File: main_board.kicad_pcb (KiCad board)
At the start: 2 copper layers, 158.5 x 153 mm, 15 parts, among them J1 MEGA_SARJ, J2 POWER, J3 I2C, J4 FREE_GPIO, J5 5V, J6 12V, J7 24V, J8 GND, J9 GND, U1 BNO055_IMU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

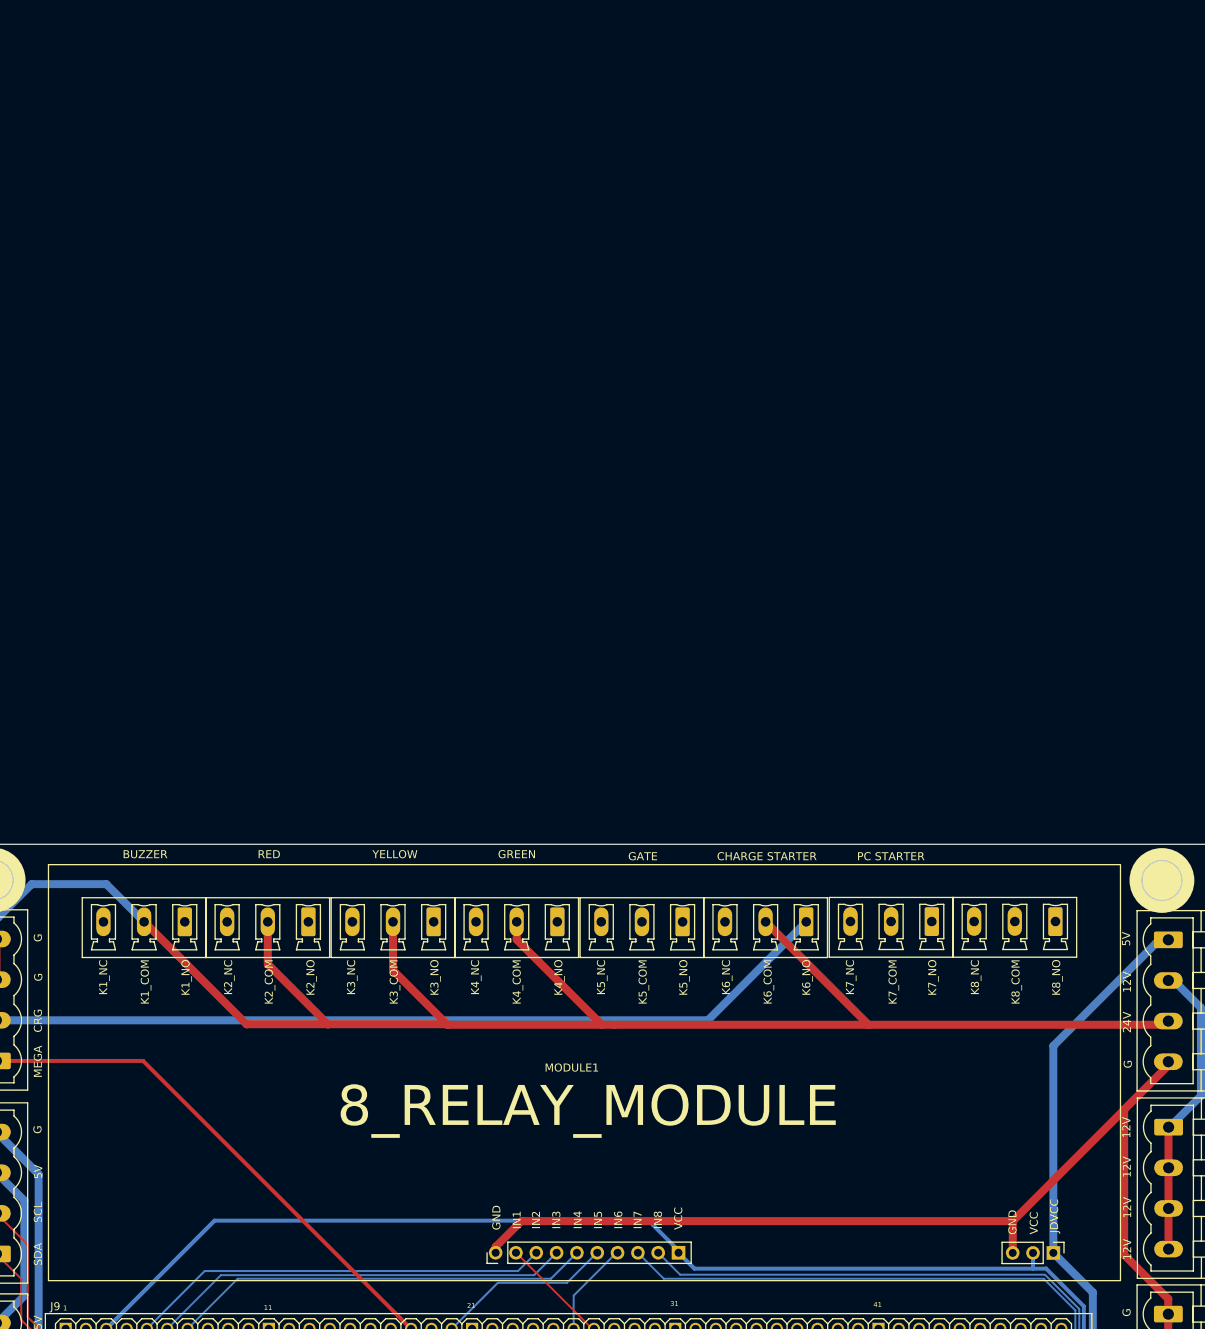
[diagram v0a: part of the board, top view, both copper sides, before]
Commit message: Deleting Relays Adding MOSFETs
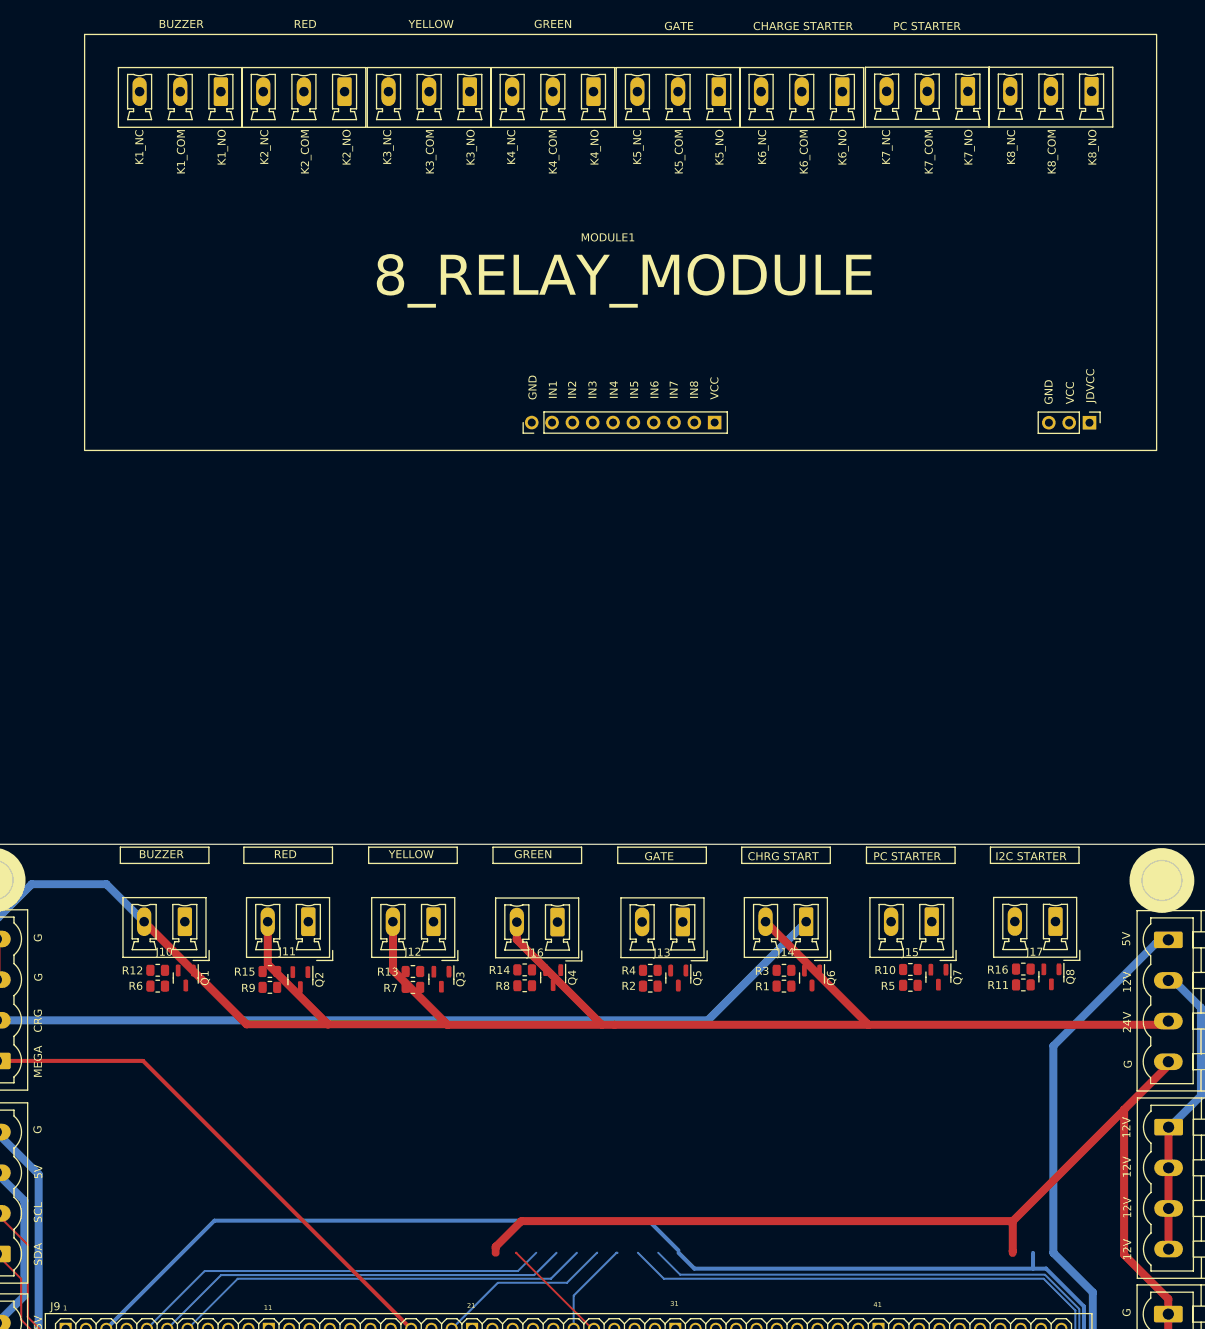
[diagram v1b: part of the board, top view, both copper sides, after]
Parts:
- added J10: Conn_01x02, Connector_Phoenix_MC_HighVoltage:PhoenixContact_MCV_1,5_2-G-5.08_1x02_P5.08mm_Vertical, F.Cu at (44.8, 26.2)
- added J11: Conn_01x02, Connector_Phoenix_MC_HighVoltage:PhoenixContact_MCV_1,5_2-G-5.08_1x02_P5.08mm_Vertical, F.Cu at (60.3, 26.2)
- added J12: Conn_01x02, Connector_Phoenix_MC_HighVoltage:PhoenixContact_MCV_1,5_2-G-5.08_1x02_P5.08mm_Vertical, F.Cu at (75.9, 26.2)
- added J13: Conn_01x02, Connector_Phoenix_MC_HighVoltage:PhoenixContact_MCV_1,5_2-G-5.08_1x02_P5.08mm_Vertical, F.Cu at (107.1, 26.2)
- added J14: Conn_01x02, Connector_Phoenix_MC_HighVoltage:PhoenixContact_MCV_1,5_2-G-5.08_1x02_P5.08mm_Vertical, F.Cu at (122.5, 26.2)
- added J15: Conn_01x02, Connector_Phoenix_MC_HighVoltage:PhoenixContact_MCV_1,5_2-G-5.08_1x02_P5.08mm_Vertical, F.Cu at (138.2, 26.2)
- added J16: Conn_01x02, Connector_Phoenix_MC_HighVoltage:PhoenixContact_MCV_1,5_2-G-5.08_1x02_P5.08mm_Vertical, F.Cu at (91.4, 26.2)
- added J17: Conn_01x02, Connector_Phoenix_MC_HighVoltage:PhoenixContact_MCV_1,5_2-G-5.08_1x02_P5.08mm_Vertical, F.Cu at (153.7, 26.2)
- added Q1: PJA3406, Package_TO_SOT_SMD:SOT-23, F.Cu at (45.0, 33.2)
- added Q2: PJA3406, Package_TO_SOT_SMD:SOT-23, F.Cu at (59.3, 33.4)
- added Q3: PJA3406, Package_TO_SOT_SMD:SOT-23, F.Cu at (76.9, 33.4)
- added Q4: PJA3406, Package_TO_SOT_SMD:SOT-23, F.Cu at (90.9, 33.2)
- added Q5: PJA3406, Package_TO_SOT_SMD:SOT-23, F.Cu at (106.5, 33.2)
- added Q6: PJA3406, Package_TO_SOT_SMD:SOT-23, F.Cu at (123.2, 33.2)
- added Q7: PJA3406, Package_TO_SOT_SMD:SOT-23, F.Cu at (139.0, 33.1)
- added Q8: PJA3406, Package_TO_SOT_SMD:SOT-23, F.Cu at (153.2, 33.1)
- added R1: 10R, Resistor_SMD:R_0805_2012Metric, F.Cu at (119.7, 34.2)
- added R10: 10K, Resistor_SMD:R_0805_2012Metric, F.Cu at (135.5, 32.2)
- added R11: 10R, Resistor_SMD:R_0805_2012Metric, F.Cu at (149.7, 34.1)
- added R12: 10K, Resistor_SMD:R_0805_2012Metric, F.Cu at (41.5, 32.3)
- added R13: 10K, Resistor_SMD:R_0805_2012Metric, F.Cu at (73.4, 32.4)
- added R14: 10K, Resistor_SMD:R_0805_2012Metric, F.Cu at (87.3, 32.2)
- added R15: 10K, Resistor_SMD:R_0805_2012Metric, F.Cu at (55.5, 32.4)
- added R16: 10K, Resistor_SMD:R_0805_2012Metric, F.Cu at (149.7, 32.1)
- added R2: 10R, Resistor_SMD:R_0805_2012Metric, F.Cu at (103.0, 34.2)
- added R3: 10K, Resistor_SMD:R_0805_2012Metric, F.Cu at (119.7, 32.3)
- added R4: 10K, Resistor_SMD:R_0805_2012Metric, F.Cu at (103.0, 32.3)
- added R5: 10R, Resistor_SMD:R_0805_2012Metric, F.Cu at (135.5, 34.1)
- added R6: 10R, Resistor_SMD:R_0805_2012Metric, F.Cu at (41.5, 34.2)
- added R7: 10R, Resistor_SMD:R_0805_2012Metric, F.Cu at (73.4, 34.4)
- added R8: 10R, Resistor_SMD:R_0805_2012Metric, F.Cu at (87.3, 34.2)
- added R9: 10R, Resistor_SMD:R_0805_2012Metric, F.Cu at (55.5, 34.4)
- moved MODULE1 103.9 mm to (98.2, -51.5)
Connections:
- MODULE1 pad 1: +5V -> unconnected-(MODULE1-Pad1)
- MODULE1 pad 10: N2HET2_10 -> unconnected-(MODULE1-Pad10)
- MODULE1 pad 11: N2HET2_8 -> unconnected-(MODULE1-Pad11)
- MODULE1 pad 12: N2HET2_13/MIBSPI2SOMI -> unconnected-(MODULE1-Pad12)
- MODULE1 pad 13: +3V3 -> unconnected-(MODULE1-Pad13)
- MODULE1 pad 15: +24V -> unconnected-(MODULE1-Pad15)
- MODULE1 pad 16: /BUZZER ALARM -> unconnected-(MODULE1-Pad16)
- MODULE1 pad 18: +24V -> unconnected-(MODULE1-Pad18)
- MODULE1 pad 19: /RED ALARM -> unconnected-(MODULE1-Pad19)
- MODULE1 pad 2: +3V3 -> unconnected-(MODULE1-Pad2)
- MODULE1 pad 21: +24V -> unconnected-(MODULE1-Pad21)
- MODULE1 pad 22: /YELLOW ALARM -> unconnected-(MODULE1-Pad22)
- MODULE1 pad 24: +24V -> unconnected-(MODULE1-Pad24)
- MODULE1 pad 25: /GREEN ALARM -> unconnected-(MODULE1-Pad25)
- MODULE1 pad 27: /KAPI_KUMANDA_SW1 -> unconnected-(MODULE1-Pad27)
- MODULE1 pad 28: /KAPI_KUMANDA_SW2 -> unconnected-(MODULE1-Pad28)
- MODULE1 pad 3: GND -> unconnected-(MODULE1-Pad3)
- MODULE1 pad 30: +24V -> unconnected-(MODULE1-Pad30)
- MODULE1 pad 31: /SARJ START -> unconnected-(MODULE1-Pad31)
- MODULE1 pad 33: /PC_ON_HEADER_GND -> unconnected-(MODULE1-Pad33)
- MODULE1 pad 34: /PC_ON_HEADER -> unconnected-(MODULE1-Pad34)
- MODULE1 pad 4: GND -> unconnected-(MODULE1-Pad4)
- MODULE1 pad 5: N2HET2_9 -> unconnected-(MODULE1-Pad5)
- MODULE1 pad 6: N2HET2_0 -> unconnected-(MODULE1-Pad6)
- MODULE1 pad 7: N2HET2_1/N2HET1_NDIS -> unconnected-(MODULE1-Pad7)
- MODULE1 pad 8: N2HET2_6 -> unconnected-(MODULE1-Pad8)
- MODULE1 pad 9: N2HET2_7/MIBSPI2NCS_0 -> unconnected-(MODULE1-Pad9)
- U5 pad 2: +3V3 -> +3.3V
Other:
- board text added: "CHRG START"
- board text added: "I2C STARTER"
